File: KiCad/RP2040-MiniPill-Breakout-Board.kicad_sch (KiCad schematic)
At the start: 4 parts, among them J1 Conn_01x20_Socket, J2 Conn_01x20_Socket, J3 Screw_Terminal_01x20, J4 Screw_Terminal_01x20

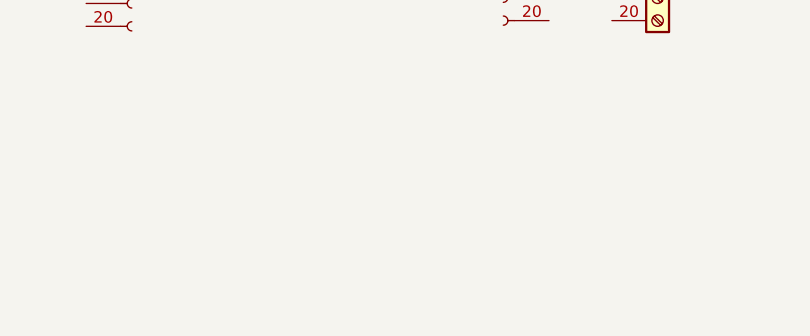
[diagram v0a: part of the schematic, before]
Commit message: adding Batteryholder
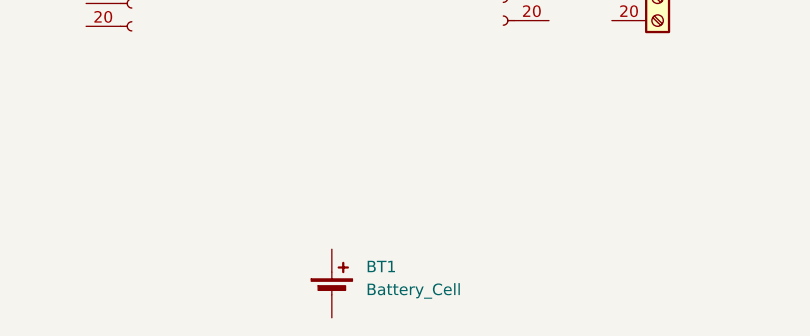
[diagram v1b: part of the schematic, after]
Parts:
- added BT1: Battery_Cell, Battery:BatteryHolder_Keystone_2460_1xAA, symbol Device:Battery_Cell
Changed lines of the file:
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@@
 	(paper "A4")
+	(symbol
+		(lib_id "Device:Battery_Cell")
+		(at 182.88 140.97 0)
+		(unit 1)
+		(exclude_from_sim no)
+		(in_bom yes)
+		(on_board yes)
+		(dnp no)
+		(fields_autoplaced yes)
+		(property "Reference" "BT1"
+			(at 186.69 137.8584 0)
+			(effects
+				(font
+					(size 1.27 1.27)
+				)
+				(justify left)
+			)
+		)
+		(property "Value" "Battery_Cell"
+			(at 186.69 140.3984 0)
+			(effects
+				(font
+					(size 1.27 1.27)
+				)
+				(justify left)
+			)
+		)
+		(property "Footprint" "Battery:BatteryHolder_Keystone_2460_1xAA"
+			(at 182.88 139.446 90)
+			(effects
+				(font
+					(size 1.27 1.27)
+				)
+				(hide yes)
+			)
+		)
+		(property "Datasheet" "~"
+			(at 182.88 139.446 90)
+			(effects
+				(font
+					(size 1.27 1.27)
+				)
+				(hide yes)
+			)
+		)
+		(property "Description" "Single-cell battery"
+			(at 182.88 140.97 0)
+			(effects
+				(font
+					(size 1.27 1.27)
+				)
+				(hide yes)
+			)
+		)
+		(pin "1"
+		)
+		(pin "2"
+		)
+		(instances
+			(project ""
+				(path "/575ab84a-8f52-4420-9d9a-fd7b17673af6"
+					(reference "BT1")
+					(unit 1)
+				)
+			)
+		)
+	)
 	(symbol
 		(lib_id "Connector:Screw_Terminal_01x20")

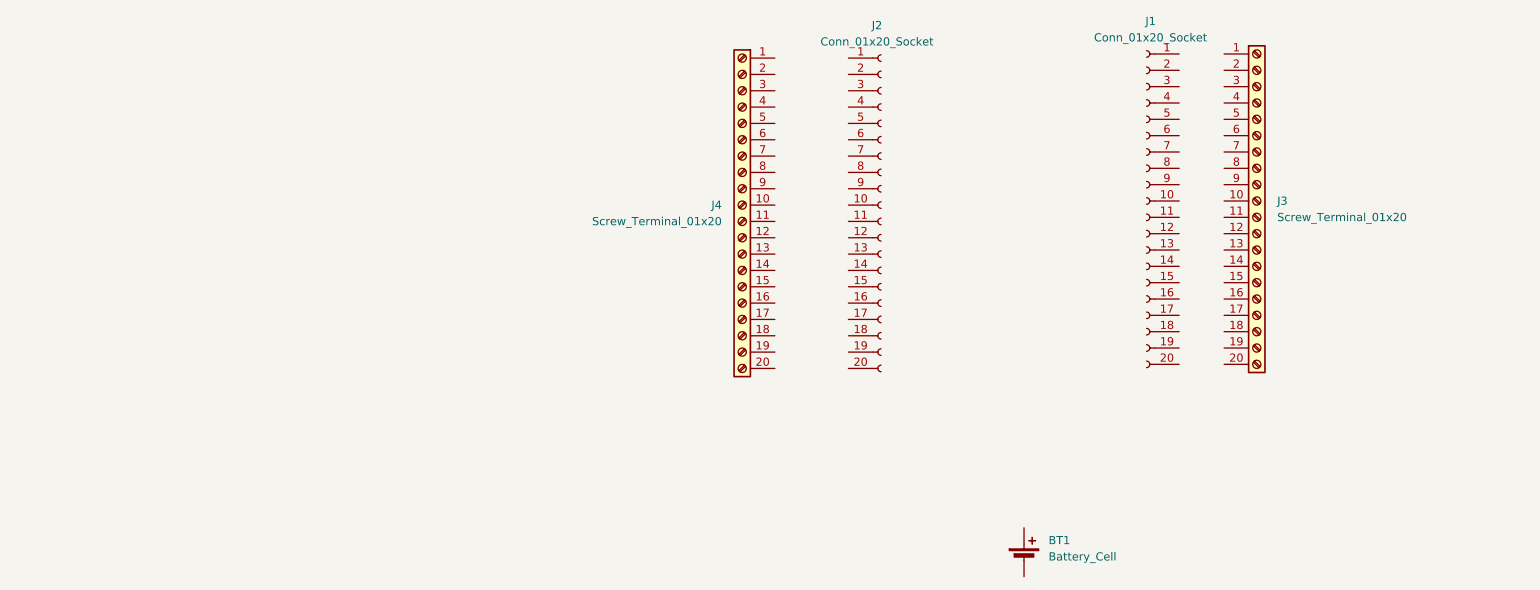
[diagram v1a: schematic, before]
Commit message: adding over and undervoltage monitoring
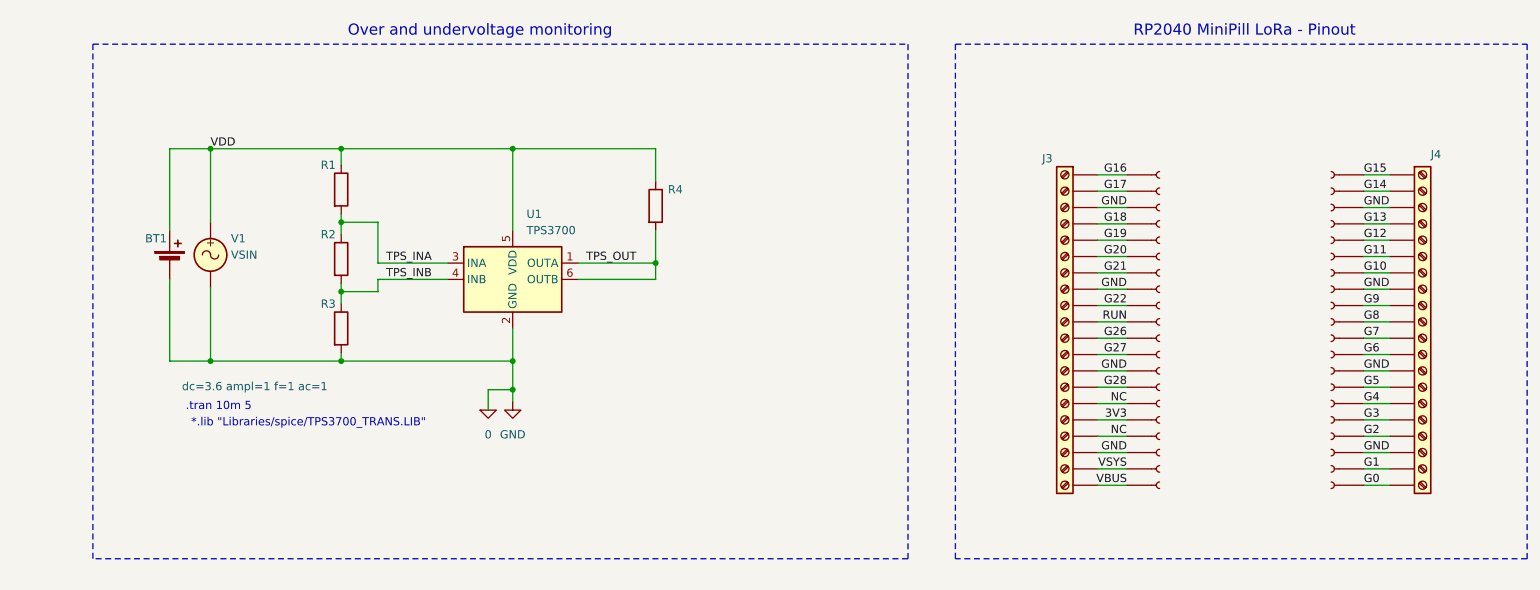
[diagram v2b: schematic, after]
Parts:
- added R1, R2, R3, R4: ${SIM.PARAMS}, symbol Device:R
- added U1: TPS3700, Package_TO_SOT_SMD:SOT-23-6, symbol Power_Supervisor:TPS3702
- added V1: VSIN, symbol Simulation_SPICE:VSIN
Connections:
- net VDD: now reaches BT1.1 (+)
- net VDD: now also R1.1, R4.1, U1.5 (VDD), V1.1
- net 0: now reaches BT1.2 (-)
- net 0: now also J1.13 (Pin_13), J1.18 (Pin_18), J1.3 (Pin_3), J1.8 (Pin_8), J2.13 (Pin_13), J2.18 (Pin_18), J2.3 (Pin_3), J2.8 (Pin_8), J3.13 (Pin_13), J3.18 (Pin_18), J3.3 (Pin_3), J3.8 (Pin_8), J4.13 (Pin_13), J4.18 (Pin_18), J4.3 (Pin_3), J4.8 (Pin_8), R3.2, U1.2 (GND), V1.2
- net G15: now reaches J4.1 (Pin_1)
- net G15: now also J2.1 (Pin_1)
- net G8: now reaches J4.10 (Pin_10)
- net G8: now also J2.10 (Pin_10)
- net G7: now reaches J4.11 (Pin_11)
- net G7: now also J2.11 (Pin_11)
- net G6: now reaches J4.12 (Pin_12)
- net G6: now also J2.12 (Pin_12)
- net G5: now reaches J4.14 (Pin_14)
- net G5: now also J2.14 (Pin_14)
- net G4: now reaches J4.15 (Pin_15)
- net G4: now also J2.15 (Pin_15)
- net G3: now reaches J4.16 (Pin_16)
- net G3: now also J2.16 (Pin_16)
- net G2: now reaches J4.17 (Pin_17)
- net G2: now also J2.17 (Pin_17)
- net G1: now reaches J4.19 (Pin_19)
- net G1: now also J2.19 (Pin_19)
- net G14: now reaches J4.2 (Pin_2)
- net G14: now also J2.2 (Pin_2)
- net G0: now reaches J4.20 (Pin_20)
- net G0: now also J2.20 (Pin_20)
- net G13: now reaches J4.4 (Pin_4)
- net G13: now also J2.4 (Pin_4)
- net G12: now reaches J4.5 (Pin_5)
- net G12: now also J2.5 (Pin_5)
- net G11: now reaches J4.6 (Pin_6)
- net G11: now also J2.6 (Pin_6)
- net G10: now reaches J4.7 (Pin_7)
- net G10: now also J2.7 (Pin_7)
- net G9: now reaches J4.9 (Pin_9)
- net G9: now also J2.9 (Pin_9)
- net G16: now reaches J1.1 (Pin_1)
- net G16: now also J3.1 (Pin_1)
- net RUN: now reaches J1.10 (Pin_10)
- net RUN: now also J3.10 (Pin_10)
- net G26: now reaches J1.11 (Pin_11)
- net G26: now also J3.11 (Pin_11)
- net G27: now reaches J1.12 (Pin_12)
- net G27: now also J3.12 (Pin_12)
- net G28: now reaches J1.14 (Pin_14)
- net G28: now also J3.14 (Pin_14)
- net NC: now reaches J1.15 (Pin_15)
- net NC: now also J1.17 (Pin_17), J3.15 (Pin_15), J3.17 (Pin_17)
- net 3V3: now reaches J1.16 (Pin_16)
- net 3V3: now also J3.16 (Pin_16)
- net VSYS: now reaches J1.19 (Pin_19)
- net VSYS: now also J3.19 (Pin_19)
- net G17: now reaches J1.2 (Pin_2)
- net G17: now also J3.2 (Pin_2)
- net VBUS: now reaches J1.20 (Pin_20)
- net VBUS: now also J3.20 (Pin_20)
- net G18: now reaches J1.4 (Pin_4)
- net G18: now also J3.4 (Pin_4)
- net G19: now reaches J1.5 (Pin_5)
- net G19: now also J3.5 (Pin_5)
- net G20: now reaches J1.6 (Pin_6)
- net G20: now also J3.6 (Pin_6)
- net G21: now reaches J1.7 (Pin_7)
- net G21: now also J3.7 (Pin_7)
- net G22: now reaches J1.9 (Pin_9)
- net G22: now also J3.9 (Pin_9)
- new net TPS_INA: R1.2, R2.1, U1.3 (INA)
- new net TPS_INB: R2.2, R3.1, U1.4 (INB)
- new net TPS_OUT: R4.2, U1.1 (OUTA), U1.6 (OUTB)
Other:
- note added: "*.lib "Libraries/spice/TPS3700_TRANS.LIB""
- note added: ".tran 10m 5"
- note added: "Over and undervoltage monitoring"
- note added: "RP2040 MiniPill LoRa - Pinout"
- moved on the sheet: BT1

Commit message: adding Simulation
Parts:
- removed V1: VSIN, symbol Simulation_SPICE:VSIN
- added C1: C, Capacitor_SMD:C_0603_1608Metric_Pad1.08x0.95mm_HandSolder, symbol Device:C
- added Q1: IRLML6402, Package_TO_SOT_SMD:SOT-23, symbol Device:Q_PMOS
- added Q2: IRLML2502, Package_TO_SOT_SMD:SOT-23, symbol Device:Q_NMOS
- added R5, R6: 50k, Resistor_SMD:R_0603_1608Metric_Pad0.98x0.95mm_HandSolder, symbol Device:R
- R1: value ${SIM.PARAMS} -> 2K; footprint (none) -> Resistor_SMD:R_0603_1608Metric_Pad0.98x0.95mm_HandSolder
- R2: value ${SIM.PARAMS} -> 100; footprint (none) -> Resistor_SMD:R_0603_1608Metric_Pad0.98x0.95mm_HandSolder
- R3: value ${SIM.PARAMS} -> 220; footprint (none) -> Resistor_SMD:R_0603_1608Metric_Pad0.98x0.95mm_HandSolder
- R4: value ${SIM.PARAMS} -> 50k; footprint (none) -> Resistor_SMD:R_0603_1608Metric_Pad0.98x0.95mm_HandSolder
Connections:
- net 3V3: now also Q1.D
- net VDD: now also C1.1, Q1.S, R5.1
- net 0 renamed GND
- net GND: now also Q2.S
- net TPS_INA: no longer names the net of R1.2, R2.1, U1.3 (INA)
- net TPS_INB: no longer names the net of R2.2, R3.1, U1.4 (INB)
- net TPS_OUT: no longer names the net of R4.2, U1.1 (OUTA), U1.6 (OUTB)
- net TPS_OUT: now also Q2.G
- new net: C1.2, Q1.G, R5.2, R6.1
- new net: Q2.D, R6.2
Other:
- note added: "Over- and Undervoltage monitoring"
- note removed: "*.lib "Libraries/spice/TPS3700_TRANS.LIB""
- note removed: ".tran 10m 5"
- note removed: "Over and undervoltage monitoring"
- title: (none) -> RP2040-MiniPill-Breakout-Board
- moved on the sheet: BT1, R1, R2, R3, R4, U1

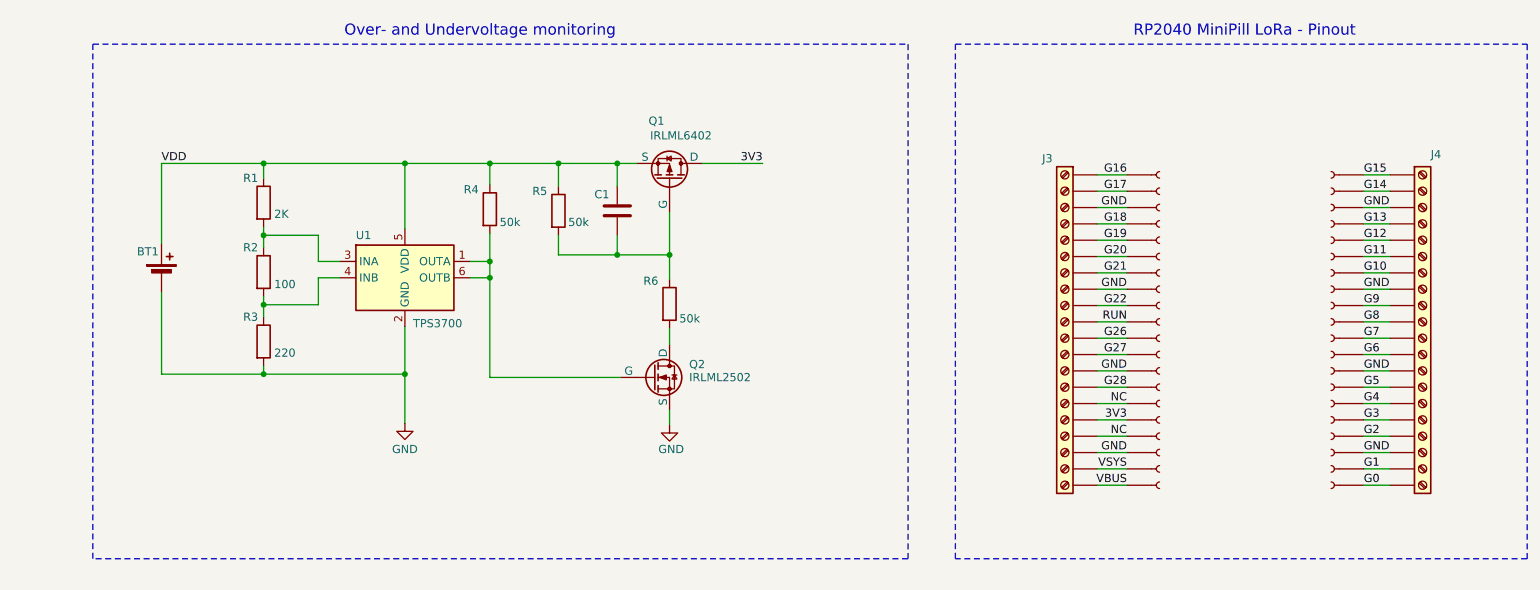
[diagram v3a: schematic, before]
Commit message: adding diode and making first placement
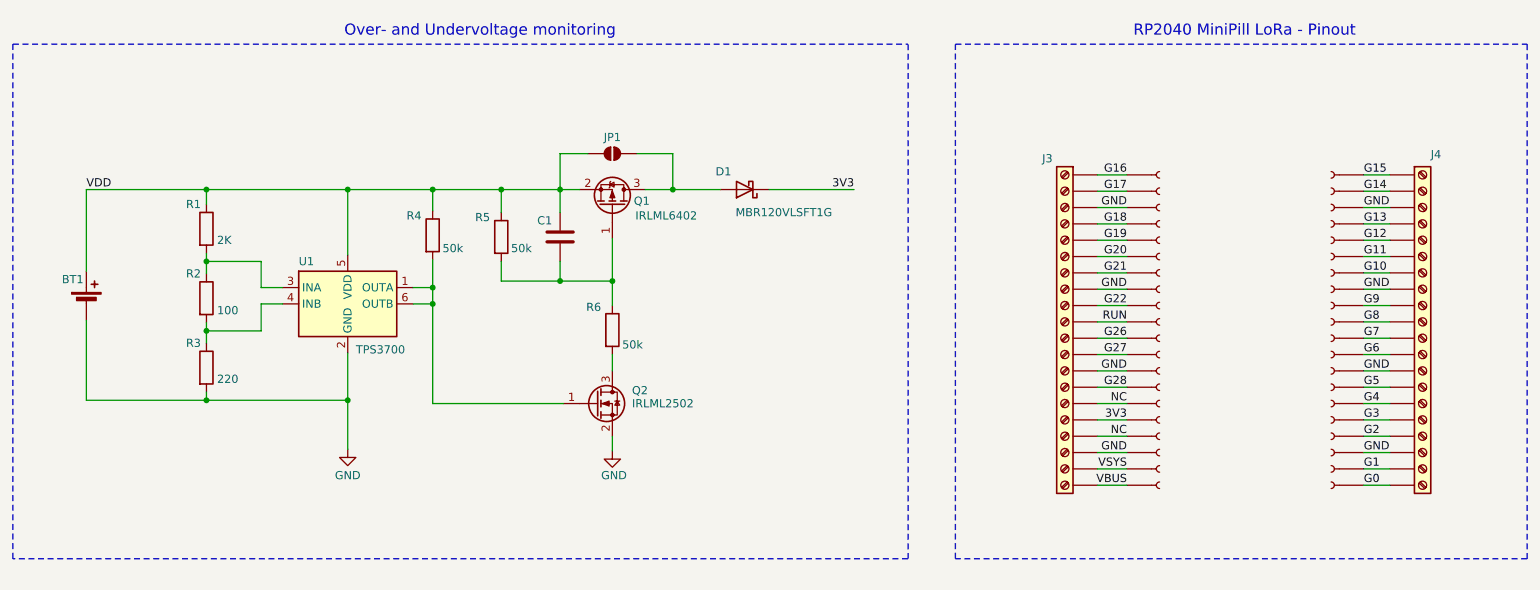
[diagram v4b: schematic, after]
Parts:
- added D1: MBR120VLSFT1G, Diode_SMD:D_SOD-123F, symbol Device:D_Schottky
- added JP1: SolderJumper_2_Open, Jumper:SolderJumper-2_P1.3mm_Open_TrianglePad1.0x1.5mm, symbol Jumper:SolderJumper_2_Open
- Q1: symbol Device:Q_PMOS -> Transistor_FET:IRLML6402
- Q2: symbol Device:Q_NMOS -> Transistor_FET:IRLML2060
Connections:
- net 3V3: now also D1.1 (K); no longer Q1.D
- net GND: now also Q2.2 (S); no longer Q2.S
- net VDD: now also Q1.2 (S), JP1.1 (A); no longer Q1.S
- net at C1.2, R5.2, R6.1: now also Q1.1 (G); no longer Q1.G
- net at R4.2, U1.1 (OUTA), U1.6 (OUTB): now also Q2.1 (G); no longer Q2.G
- net at R6.2: now also Q2.3 (D); no longer Q2.D
- new net: D1.2 (A), JP1.2 (B), Q1.3 (D)
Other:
- moved on the sheet: BT1, C1, Q1, Q2, R1, R2, R3, R4, R5, R6, U1

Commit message: adding LCSC Parts
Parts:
- U1: LCSC (none) -> C33002
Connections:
- net NC: no longer names the net of J1.15 (Pin_15), J3.15 (Pin_15)
- net NC: no longer J1.17 (Pin_17), J3.17 (Pin_17)
- new net: J1.17 (Pin_17), J3.17 (Pin_17)
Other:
- note added: "NC"
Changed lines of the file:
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@@
 		)
 	)
+	(text "NC"
+		(exclude_from_sim no)
+		(at 198.628 120.904 0)
+		(effects
+			(font
+				(size 1.27 1.27)
+			)
+			(justify right)
+		)
+	)
 	(text "Over- and Undervoltage monitoring"
 		(exclude_from_sim no)
@@
 		)
 	)
+	(text "NC"
+		(exclude_from_sim no)
+		(at 198.628 115.824 0)
+		(effects
+			(font
+				(size 1.27 1.27)
+			)
+			(justify right)
+		)
+	)
 	(text "RP2040 MiniPill LoRa - Pinout"
 		(exclude_from_sim no)
@@
 		)
 	)
-	(label "NC"
-		(at 198.882 116.586 180)
-		(effects
-			(font
-				(size 1.27 1.27)
-			)
-			(justify right bottom)
-		)
-	)
 	(label "G8"
 		(at 235.712 103.886 0)
@@
 		)
 	)
-	(label "NC"
-		(at 198.882 121.666 180)
-		(effects
-			(font
-				(size 1.27 1.27)
-			)
-			(justify right bottom)
-		)
-	)
 	(symbol
 		(lib_id "Transistor_FET:IRLML6402")
@@
 			)
 		)
-		(property "Sim.Library" "Libraries/spice/TPS3700_TRANS_SIMPL.LIB"
-			(at 77.724 101.092 0)
-			(effects
-				(font
-					(size 1.27 1.27)
-				)
-				(hide yes)
-			)
-		)
-		(property "Sim.Name" "TPS3700_SIMPL"
-			(at 77.724 101.092 0)
-			(effects
-				(font
-					(size 1.27 1.27)
-				)
-				(hide yes)
-			)
-		)
-		(property "Sim.Device" "SUBCKT"
-			(at 77.724 101.092 0)
-			(effects
-				(font
-					(size 1.27 1.27)
-				)
-				(hide yes)
-			)
-		)
-		(property "Sim.Pins" "1=OUTA 2=GND 3=INA 4=INB 5=VDD 6=OUTB"
+		(property "LCSC" "C33002"
 			(at 77.724 101.092 0)
 			(effects

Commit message: adding some LCSC parts and making some finetuning
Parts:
- BT1: LCSC (none) -> C5290181
- C1: value C -> 100n; LCSC (none) -> C14663
- D1: LCSC (none) -> C223608
- Q1: LCSC (none) -> C2593
- Q2: LCSC (none) -> C2589
- R2: LCSC (none) -> C22775
- R3: LCSC (none) -> C22962
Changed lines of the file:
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@@
+			)
+		)
+		(property "LCSC" "C2593"
+			(at 118.872 85.852 90)
+			(effects
+				(font
+					(size 1.27 1.27)
+				)
+				(hide yes)
 			)
 		)
@@
 			)
 		)
+		(property "LCSC" "C22775"
+			(at 55.753 100.203 0)
+			(effects
+				(font
+					(size 1.27 1.27)
+				)
+				(hide yes)
+			)
+		)
 		(pin "1"
 		)
@@
 			)
 		)
+		(property "LCSC" "C5290181"
+			(at 37.084 101.092 0)
+			(effects
+				(font
+					(size 1.27 1.27)
+				)
+				(hide yes)
+			)
+		)
 		(pin "1"
 		)
@@
 			)
 		)
+		(property "LCSC" "C22962"
+			(at 55.753 110.998 0)
+			(effects
+				(font
+					(size 1.27 1.27)
+				)
+				(hide yes)
+			)
+		)
 		(pin "1"
 		)
@@
 			)
 		)
-		(property "Value" "C"
-			(at 113.792 91.9479 0)
-			(effects
-				(font
-					(size 1.27 1.27)
-				)
-				(justify left)
-				(hide yes)
+		(property "Value" "100n"
+			(at 113.03 92.456 0)
+			(effects
+				(font
+					(size 1.27 1.27)
+				)
+				(justify left)
 			)
 		)
@@
 		)
 		(property "Description" "Unpolarized capacitor"
+			(at 110.744 90.678 0)
+			(effects
+				(font
+					(size 1.27 1.27)
+				)
+				(hide yes)
+			)
+		)
+		(property "LCSC" "C14663"
 			(at 110.744 90.678 0)
 			(effects
@@
 			)
 		)
+		(property "LCSC" "C2589"
+			(at 116.332 116.586 0)
+			(effects
+				(font
+					(size 1.27 1.27)
+				)
+				(hide yes)
+			)
+		)
 		(pin "3"
 		)
@@
 			(at 139.446 83.312 0)
 			(effects
+				(font
+					(size 1.27 1.27)
+				)
+				(hide yes)
+			)
+		)
+		(property "LCSC" "C223608"
+			(at 139.446 83.312 0)
+			(effects

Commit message: adding LCSC No for some parts
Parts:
- J3, J4: LCSC (none) -> C915914 (4x)
- R1: LCSC (none) -> C22975
- R4, R5, R6: LCSC (none) -> C861451
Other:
- company: (none) -> OpenLab-Saar
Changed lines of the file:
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@@
 		(title "RP2040-MiniPill-Breakout-Board")
 		(date "2025-09-29")
+		(company "OpenLab-Saar")
 	)
 	(rectangle
@@
 			)
 		)
+		(property "LCSC" "C861451"
+			(at 90.932 90.424 0)
+			(effects
+				(font
+					(size 1.27 1.27)
+				)
+				(hide yes)
+			)
+		)
 		(pin "1"
 		)
@@
 			)
 		)
+		(property "LCSC" "C861451"
+			(at 101.6 90.678 0)
+			(effects
+				(font
+					(size 1.27 1.27)
+				)
+				(hide yes)
+			)
+		)
 		(pin "1"
 		)
@@
 			)
 		)
+		(property "LCSC" "C915914 (4x)"
+			(at 244.856 103.886 0)
+			(effects
+				(font
+					(size 1.27 1.27)
+				)
+				(hide yes)
+			)
+		)
 		(pin "19"
 		)
@@
 			)
 		)
+		(property "LCSC" "C915914 (4x)"
+			(at 189.23 103.886 0)
+			(effects
+				(font
+					(size 1.27 1.27)
+				)
+				(hide yes)
+			)
+		)
 		(pin "19"
 		)
@@
 			)
 		)
+		(property "LCSC" "C861451"
+			(at 118.872 105.156 0)
+			(effects
+				(font
+					(size 1.27 1.27)
+				)
+				(hide yes)
+			)
+		)
 		(pin "1"
 		)
@@
 			(at 55.753 89.408 0)
 			(effects
+				(font
+					(size 1.27 1.27)
+				)
+				(hide yes)
+			)
+		)
+		(property "LCSC" "C22975"
+			(at 55.753 89.408 0)
+			(effects

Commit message: adding custom Drawing Sheet and making some finetuning
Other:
- title: RP2040-MiniPill-Breakout-Board -> RP2040 MiniPill BreakoutBoard
